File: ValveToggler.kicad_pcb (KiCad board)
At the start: 4 copper layers, 75 x 50 mm, 51 parts, among them J1 24V IN, J17 MODE (24V), J2 Coil2, J3 Coil1, Q1 IRFZ24N, Q3 IRFZ24N, Q4 2N7000, Q7 2N7000, U2 NE555P, U3 L7812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

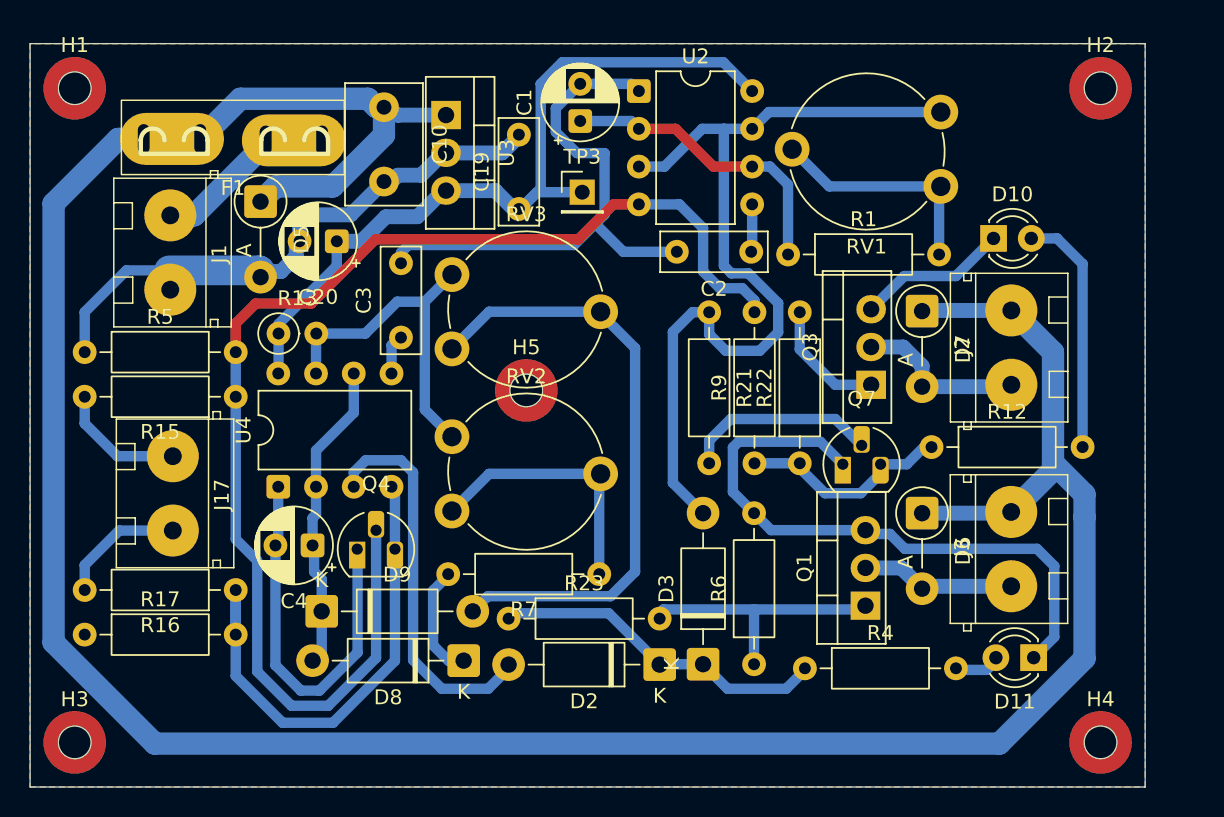
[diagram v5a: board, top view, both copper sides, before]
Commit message: Fix mos1 not turning fully on (rework leds), Fix swapped text, Add changelog
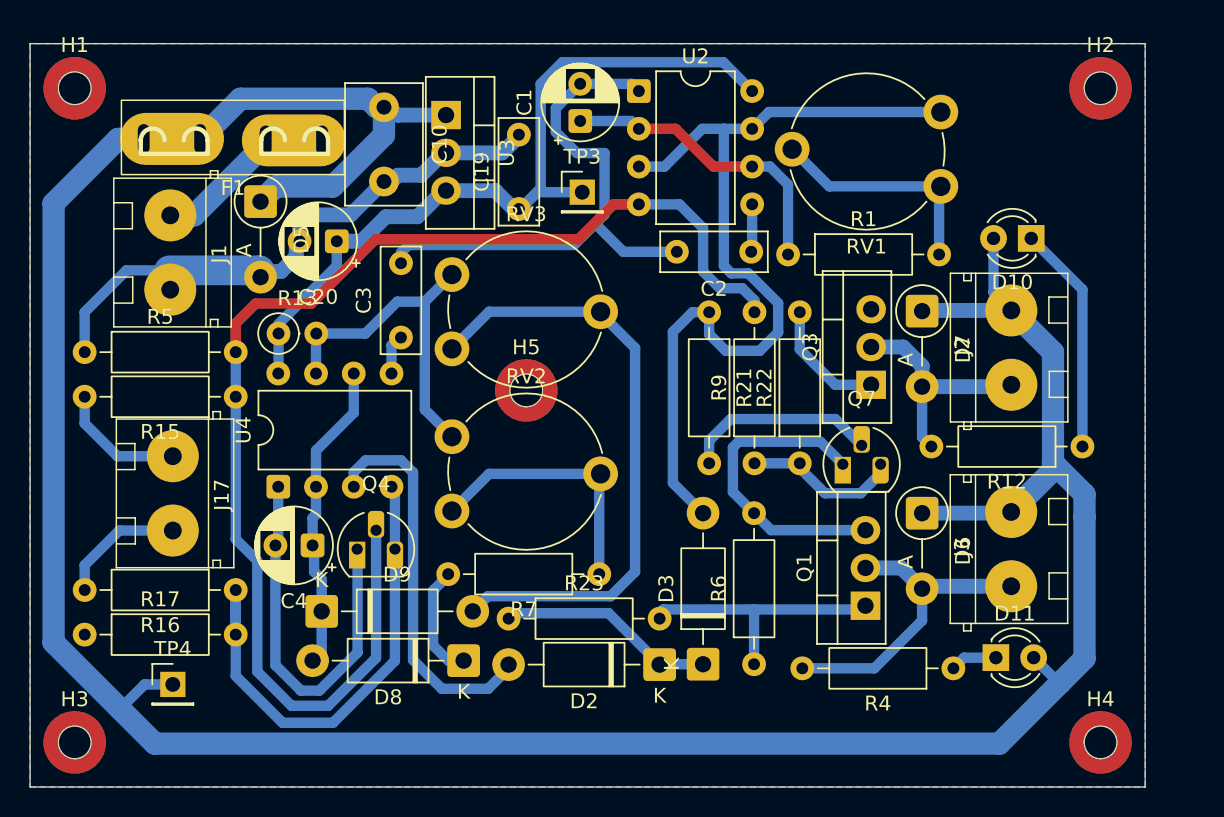
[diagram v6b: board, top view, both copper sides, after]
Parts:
- added TP4: 24V, Connector_PinHeader_2.54mm:PinHeader_1x01_P2.54mm_Vertical, F.Cu at (52.6, 88.1)
- R1: value 1k5_f-min -> 1k5_f-max
- R12, R4: value 1k5 -> 3k3
- R13: value 1k5_t-onMin -> 2k2_t-onMin
- RV1: value 50k_freq1 -> 100k_freq
- RV3: value 50k_t-on -> 10k_t-on
- moved R12 10.1 mm to (113.8, 72.1), turned to 180 degrees
- moved R4 9.99 mm to (105.1, 87.0), turned to 180 degrees
- moved D10 2.54 mm to (110.3, 58.1), turned to 180 degrees
- moved D11 2.54 mm to (108.0, 86.3), turned to 0 degrees
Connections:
- D10 pad 1: GND -> Net-(D10-K)
- D10 pad 2: Net-(D10-A) -> +24V
- D11 pad 1: GND -> Net-(D11-K)
- D11 pad 2: Net-(D11-A) -> +24V
- D6 pad 2: Net-(D6-A) -> /Drain1
- D7 pad 2: Net-(D7-A) -> /Drain2
- J2 pad 1: Net-(D7-A) -> /Drain2
- J3 pad 1: Net-(D6-A) -> /Drain1
- Q1 pad 2: Net-(D6-A) -> /Drain1
- Q3 pad 2: Net-(D7-A) -> /Drain2
- R12 pad 1: /MOS2 -> Net-(D10-K)
- R12 pad 2: Net-(D10-A) -> /Drain2
- R4 pad 1: /MOS1 -> Net-(D11-K)
- R4 pad 2: Net-(D11-A) -> /Drain1
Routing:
- net GND: track 154.0 -> 123.4 mm
- net /Drain1: track 0.00 -> 22.0 mm
- net Net-(D10-A): track 16.5 -> 0.00 mm
- net /Drain2: track 0.00 -> 15.7 mm
- net Net-(D10-K): track 0.00 -> 15.4 mm
- net +24V: track 187.8 -> 199.9 mm
- net Net-(D7-A): track 11.4 -> 0.00 mm
- net Net-(D6-A): track 10.4 -> 0.00 mm
- net /MOS1: track 22.9 -> 14.7 mm
- net /MOS2: track 14.6 -> 10.7 mm
- net Net-(D11-A): track 3.27 -> 0.00 mm
- net Net-(D11-K): track 0.00 -> 3.16 mm
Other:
- board text added: "Layer User7: Marked pads to solder on top side as well:"
- board text added: "M2 M1"
- board text added: "max 3A"
- board text removed: "Layer User7: Marked pads to solder on top side"
- board text removed: "M1 M2"
